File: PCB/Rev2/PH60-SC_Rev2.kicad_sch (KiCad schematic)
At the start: 43 parts, among them J1 USB_C_Receptacle_USB2.0_14P, J2 Conn_01x02_Pin, J3 Conn_01x02_Pin, U1 nRF52840, X1 32.768kHz, X2 Crystal_Generic

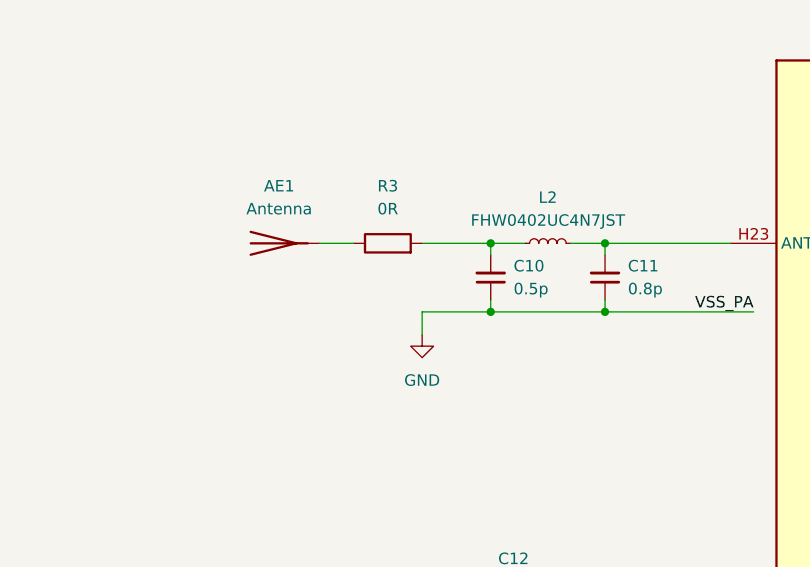
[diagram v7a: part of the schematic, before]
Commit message: Change RGB and antenna
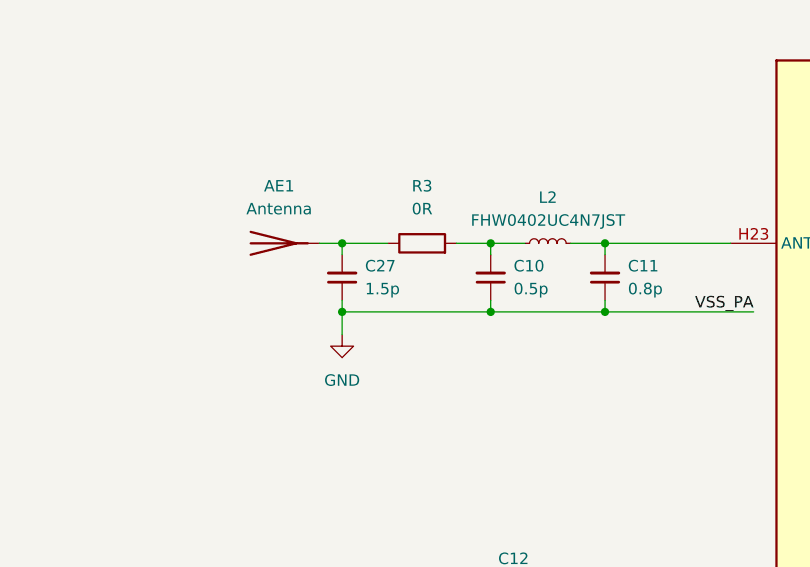
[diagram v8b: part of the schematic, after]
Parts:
- added C27: 1.5p, Capacitor_SMD:C_0402_1005Metric, symbol Device:C_Small
- R3: footprint PCM_Resistor_SMD_AKL:R_0603_1608Metric -> Capacitor_SMD:C_0402_1005Metric
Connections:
- net GND: now also C27.1
- net at AE1.1 (A), R3.1: now also C27.2
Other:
- moved on the sheet: R3
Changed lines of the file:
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@@
 	)
 	(junction
+		(at 147.32 104.14)
+		(diameter 0)
+		(color 0 0 0 0)
+	)
+	(junction
 		(at 213.36 53.34)
 		(diameter 0)
@@
 	)
 	(junction
+		(at 147.32 111.76)
+		(diameter 0)
+		(color 0 0 0 0)
+	)
+	(junction
 		(at 165.1 50.8)
 		(diameter 0)
@@
 	(wire
 		(pts
-			(xy 156.21 111.76) (xy 163.83 111.76)
+			(xy 213.36 53.34) (xy 218.44 53.34)
 		)
 		(stroke
@@
 	(wire
 		(pts
-			(xy 213.36 53.34) (xy 218.44 53.34)
+			(xy 172.72 143.51) (xy 181.61 143.51)
 		)
 		(stroke
@@
 	(wire
 		(pts
-			(xy 172.72 143.51) (xy 181.61 143.51)
+			(xy 228.6 53.34) (xy 226.06 53.34)
 		)
 		(stroke
@@
 	(wire
 		(pts
-			(xy 228.6 53.34) (xy 226.06 53.34)
+			(xy 228.6 53.34) (xy 228.6 60.96)
 		)
 		(stroke
@@
 	(wire
 		(pts
-			(xy 228.6 53.34) (xy 228.6 60.96)
+			(xy 220.98 226.06) (xy 223.52 226.06)
 		)
 		(stroke
@@
 	(wire
 		(pts
-			(xy 220.98 226.06) (xy 223.52 226.06)
+			(xy 147.32 111.76) (xy 163.83 111.76)
 		)
 		(stroke
@@
 	(wire
 		(pts
+			(xy 147.32 110.49) (xy 147.32 111.76)
+		)
+		(stroke
+			(width 0)
+			(type default)
+		)
+	)
+	(wire
+		(pts
 			(xy 34.29 67.31) (xy 34.29 68.58)
 		)
@@
 	(wire
 		(pts
+			(xy 147.32 105.41) (xy 147.32 104.14)
+		)
+		(stroke
+			(width 0)
+			(type default)
+		)
+	)
+	(wire
+		(pts
 			(xy 226.06 226.06) (xy 226.06 220.98)
 		)
@@
 	(wire
 		(pts
-			(xy 156.21 104.14) (xy 163.83 104.14)
+			(xy 160.02 104.14) (xy 163.83 104.14)
 		)
 		(stroke
@@
 	(wire
 		(pts
-			(xy 156.21 111.76) (xy 156.21 114.3)
+			(xy 147.32 111.76) (xy 147.32 114.3)
 		)
 		(stroke
@@
 	(wire
 		(pts
-			(xy 144.78 104.14) (xy 148.59 104.14)
+			(xy 144.78 104.14) (xy 147.32 104.14)
 		)
 		(stroke
@@
 	(wire
 		(pts
+			(xy 147.32 104.14) (xy 152.4 104.14)
+		)
+		(stroke
+			(width 0)
+			(type default)
+		)
+	)
+	(wire
+		(pts
 			(xy 228.6 66.04) (xy 228.6 78.74)
 		)
@@
 	(symbol
 		(lib_id "Device:R")
-		(at 152.4 104.14 90)
+		(at 156.21 104.14 90)
 		(unit 1)
 		(exclude_from_sim no)
@@
 		(fields_autoplaced yes)
 		(property "Reference" "R3"
-			(at 152.4 97.79 90)
+			(at 156.21 97.79 90)
 			(effects
 				(font
@@
 		)
 		(property "Value" "0R"
-			(at 152.4 100.33 90)
+			(at 156.21 100.33 90)
 			(effects
 				(font
@@
 			)
 		)
-		(property "Footprint" "PCM_Resistor_SMD_AKL:R_0603_1608Metric"
-			(at 152.4 105.918 90)
+		(property "Footprint" "Capacitor_SMD:C_0402_1005Metric"
+			(at 156.21 105.918 90)
 			(effects
 				(font
@@
 		)
 		(property "Datasheet" "~"
-			(at 152.4 104.14 0)
+			(at 156.21 104.14 0)
 			(effects
 				(font
@@
 		)
 		(property "Description" "Resistor"
-			(at 152.4 104.14 0)
+			(at 156.21 104.14 0)
 			(effects
 				(font
@@
 	(symbol
 		(lib_id "Device:C_Small")
+		(at 147.32 107.95 180)
+		(unit 1)
+		(exclude_from_sim no)
+		(in_bom yes)
+		(on_board yes)
+		(dnp no)
+		(fields_autoplaced yes)
+		(property "Reference" "C27"
+			(at 149.86 106.6735 0)
+			(effects
+				(font
+					(size 1.27 1.27)
+				)
+				(justify right)
+			)
+		)
+		(property "Value" "1.5p"
+			(at 149.86 109.2135 0)
+			(effects
+				(font
+					(size 1.27 1.27)
+				)
+				(justify right)
+			)
+		)
+		(property "Footprint" "Capacitor_SMD:C_0402_1005Metric"
+			(at 147.32 107.95 0)
+			(effects
+				(font
+					(size 1.27 1.27)
+				)
+				(hide yes)
+			)
+		)
+		(property "Datasheet" "~"
+			(at 147.32 107.95 0)
+			(effects
+				(font
+					(size 1.27 1.27)
+				)
+				(hide yes)
+			)
+		)
+		(property "Description" "Unpolarized capacitor, small symbol"
+			(at 147.32 107.95 0)
+			(effects
+				(font
+					(size 1.27 1.27)
+				)
+				(hide yes)
+			)
+		)
+		(pin "2"
+		)
+		(pin "1"
+		)
+		(instances
+			(project "PH60-SC_Rev2"
+				(path "/dca0f898-8fdb-4522-a51d-f4f4238906e7"
+					(reference "C27")
+					(unit 1)
+				)
+			)
+		)
+	)
+	(symbol
+		(lib_id "Device:C_Small")
 		(at 218.44 63.5 0)
 		(unit 1)
@@
 	(symbol
 		(lib_id "power:GND")
-		(at 156.21 114.3 0)
+		(at 147.32 114.3 0)
 		(unit 1)
 		(exclude_from_sim no)
@@
 		(fields_autoplaced yes)
 		(property "Reference" "#PWR08"
-			(at 156.21 120.65 0)
+			(at 147.32 120.65 0)
 			(effects
 				(font
@@
 		)
 		(property "Value" "GND"
-			(at 156.21 119.38 0)
+			(at 147.32 119.38 0)
 			(effects
 				(font
@@
 		)
 		(property "Footprint" ""
-			(at 156.21 114.3 0)
+			(at 147.32 114.3 0)
 			(effects
 				(font
@@
 		)
 		(property "Datasheet" ""
-			(at 156.21 114.3 0)
+			(at 147.32 114.3 0)
 			(effects
 				(font
@@
 		)
 		(property "Description" "Power symbol creates a global label with name \"GND\" , ground"
-			(at 156.21 114.3 0)
+			(at 147.32 114.3 0)
 			(effects
 				(font
